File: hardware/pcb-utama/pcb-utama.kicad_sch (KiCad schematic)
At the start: 0 parts

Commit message: Skematik PCB utama lengkap (ERC 0) dari generator
- hardware/tools/gen_sch_utama.py + kisym.py: skematik 5 blok (daya, driver motor, layar/tombol/buzzer, ESP32,
  J5 ke PCB sensor), 21 komponen, footprint terisi; netlist dicek terhadap tabel pin CLAUDE.md (0 salah)
- hardware/pcb-utama/pcb-utama-skematik.pdf
- README PCB utama, CLAUDE.md, handover, log kerja diperbarui

Co-Authored-By: Claude Opus 5.5 <noreply@anthropic.com>
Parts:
- added BZ1: Buzzer aktif 5V, Buzzer_Beeper:Buzzer_12x9.5RM7.6, symbol Device:Buzzer
- added C1: 100uF 16V, Capacitor_THT:CP_Radial_D6.3mm_P2.50mm, symbol Device:C_Polarized
- added D1: 1N5819, Diode_THT:D_DO-41_SOD81_P10.16mm_Horizontal, symbol Device:D_Schottky
- added J1: Baterai (P+/P- BMS), Connector_JST:JST_XH_B2B-XH-A_1x02_P2.50mm_Vertical, symbol Connector_Generic:Conn_01x02
- added J2: Motor kiri + encoder, Connector_JST:JST_PH_B6B-PH-K_1x06_P2.00mm_Vertical, symbol Connector_Generic:Conn_01x06
- added J3: Motor kanan + encoder, Connector_JST:JST_PH_B6B-PH-K_1x06_P2.00mm_Vertical, symbol Connector_Generic:Conn_01x06
- added J4: OLED 0,96 I2C, Connector_PinSocket_2.54mm:PinSocket_1x04_P2.54mm_Vertical, symbol Connector_Generic:Conn_01x04
- added J5: Kabel PCB sensor (= J1 sensor), Connector_JST:JST_XH_B8B-XH-A_1x08_P2.50mm_Vertical, symbol Connector_Generic:Conn_01x08
- added Q1: S8050, Package_TO_SOT_THT:TO-92_Inline, symbol Transistor_BJT:S8050
- added R1: 100k, Resistor_THT:R_Axial_DIN0207_L6.3mm_D2.5mm_P7.62mm_Horizontal, symbol Device:R
- added R2: 33k, Resistor_THT:R_Axial_DIN0207_L6.3mm_D2.5mm_P7.62mm_Horizontal, symbol Device:R
- added R3: 1k, Resistor_THT:R_Axial_DIN0207_L6.3mm_D2.5mm_P7.62mm_Horizontal, symbol Device:R
- added R4, R5, R6: 10k, Resistor_THT:R_Axial_DIN0207_L6.3mm_D2.5mm_P7.62mm_Horizontal, symbol Device:R
- added SW1: Saklar geser, Button_Switch_THT:SW_Slide_SPDT_Angled_CK_OS102011MA1Q, symbol Switch:SW_SPDT
- added SW2: Tombol A, Button_Switch_THT:SW_PUSH_6mm, symbol Switch:SW_Push
- added SW3: Tombol B, Button_Switch_THT:SW_PUSH_6mm, symbol Switch:SW_Push
- added U1: ESP32 DevKit 30 pin, ltm:ESP32_DevKit_30P_W25.4, symbol ltm:ESP32_DevKit_30
- added U2: TB6612 modul, ltm:TB6612_Module_2x8_W15.24, symbol ltm:TB6612_Module
- added U3: MP1584 (set 5,0 V), ltm:MP1584_Module, symbol ltm:MP1584_Module
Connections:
- new net: BZ1.2 (-), Q1.3 (C)
- new net: Q1.2 (B), R3.2, R4.1
- new net +3V3: J2.2 (Pin_2), J3.2 (Pin_2), J4.2 (Pin_2), J5.2 (Pin_2), R5.1, R6.1, U1.30 (3V3), U2.10 (VCC)
- new net +5V: BZ1.1 (+), D1.1 (K), J5.1 (Pin_1), U1.15 (VIN)
- new net +5V_BUCK: D1.2 (A), U3.3 (OUT+)
- new net AIN1: U1.23 (GPIO5), U2.3 (AIN1)
- new net AIN2: U1.24 (GPIO17/TX2), U2.2 (AIN2)
- new net BAT+: J1.1 (Pin_1), SW1.1 (A)
- new net BIN1: U1.26 (GPIO4), U2.5 (BIN1)
- new net BIN2: U1.28 (GPIO15), U2.6 (BIN2)
- new net BTN_A: R5.2, SW2.1, U1.4 (GPIO34)
- new net BTN_B: R6.2, SW3.1, U1.5 (GPIO35)
- new net BUZ: R3.1, U1.12 (GPIO12)
- new net ENC_L_A: J2.3 (Pin_3), U1.13 (GPIO13)
- new net ENC_L_B: J2.4 (Pin_4), U1.11 (GPIO14)
- new net ENC_R_A: J3.3 (Pin_3), U1.16 (GPIO23)
- new net ENC_R_B: J3.4 (Pin_4), U1.21 (GPIO19)
- new net GND: C1.2, J1.2 (Pin_2), J2.5 (Pin_5), J3.5 (Pin_5), J4.1 (Pin_1), J5.3 (Pin_3), Q1.1 (E), R2.2, R4.2, SW2.2, SW3.2, U1.14 (GND), U1.29 (GND), U2.11 (GND), U2.16 (GND), U2.8 (GND), U3.2 (IN-), U3.4 (OUT-)
- new net ML_N: J2.6 (Pin_6), U2.13 (AO2)
- new net ML_P: J2.1 (Pin_1), U2.12 (AO1)
- new net MR_N: J3.6 (Pin_6), U2.14 (BO2)
- new net MR_P: J3.1 (Pin_1), U2.15 (BO1)
- new net MUX_S0: J5.7 (Pin_7), U1.9 (GPIO26)
- new net MUX_S1: J5.6 (Pin_6), U1.8 (GPIO25)
- new net MUX_S2: J5.5 (Pin_5), U1.7 (GPIO33)
- new net MUX_S3: J5.4 (Pin_4), U1.6 (GPIO32)
- new net MUX_SIG: J5.8 (Pin_8), U1.2 (GPIO36/VP)
- new net PWMA: U1.22 (GPIO18), U2.1 (PWMA)
- new net PWMB: U1.25 (GPIO16/RX2), U2.7 (PWMB)
- new net SCL: J4.3 (Pin_3), U1.17 (GPIO22)
- new net SDA: J4.4 (Pin_4), U1.20 (GPIO21)
- new net STBY: U1.27 (GPIO2), U2.4 (STBY)
- new net VBAT: C1.1, R1.1, SW1.2 (B), U2.9 (VM), U3.1 (IN+)
- new net VBAT_SENSE: R1.2, R2.1, U1.3 (GPIO39/VN)
- no-connect marks 0 -> 5
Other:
- note added: "1. DAYA (wiring diagram blok 1)"
- note added: "2. DRIVER MOTOR + MOTOR (wiring diagram blok 2)"
- note added: "3. LAYAR, TOMBOL, BUZZER (wiring diagram blok 3)"
- note added: "4. ESP32 DEVKIT (otak)"
- note added: "5. KABEL KE PCB SENSOR (wiring diagram blok 4)"
- note added: "C1 dekat pin VM TB6612"
- note added: "Cek urutan pin modul OLED (ada yang VCC dulu baru GND)"
- note added: "D1: cegah arus balik saat USB dicolok"
- note added: "Di PCB: J5 sejajar tepi kanan hidung, pin 1 di ujung belakang"
- note added: "EN, GPIO27, TX0, RX0: tidak dipakai (X)"
- note added: "Footprint W25.4: ukur jarak baris pin modul (22,86 mm -> W22.86)"
- note added: "GPIO2 (STBY) dan GPIO12 (BUZ) harus LOW saat boot"
- note added: "GPIO34/35/36/39: hanya input"
- note added: "Ikuti NOMOR pin: pin 4-7 terbalik dari urutan nama (S3 dulu)"
- note added: "J1 = P+/P- BMS (baterai 2S di rangka)"
- note added: "J2/J3 = JST PH 6 pin. Encoder tanpa resistor (firmware INPUT_PULLUP)."
- note added: "J5 = JST XH 8 pin, urutan pin SAMA dengan J1 PCB sensor (kabel lurus, pin n ke pin n)"
- note added: "PWR_FLAG: daya VBAT, +5V, GND datang dari konektor/dioda"
- note added: "Q1 TO-92: cek urutan E-B-C"
- note added: "R4 menjaga GPIO12 LOW saat boot (syarat boot ESP32)"
- note added: "R5/R6 wajib: GPIO34/35 tanpa pull-up internal"
- note added: "SW1: kaki tengah (B) = VBAT"
- note added: "Set MP1584 ke 5,0 V dulu sebelum ESP32 dipasang"
- note added: "Urutan 6 kabel motor N20 beda tiap penjual: cek sebelum crimp."
- note added: "Urutan pin modul TB6612 beda tiap penjual: cocokkan dengan modul yang dibeli."
- note added: "VBAT_SENSE ke GPIO39 (ADC1)"
- note added: "VM = VBAT (7,4 V) langsung, VCC = 3,3 V logika. AO ke motor kiri, BO ke motor kanan."

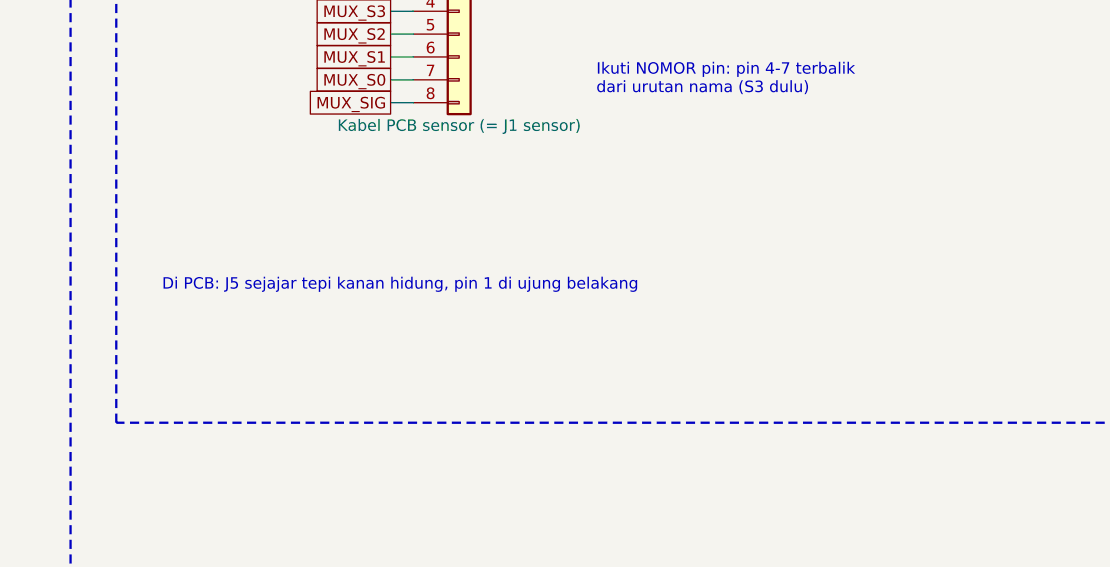
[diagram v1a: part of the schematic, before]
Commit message: Outline PCB utama bentuk mobil F1
Pilihan user dari 3 opsi: sidepod lebar, pinggang lengkung di antara roda,
hidung panjang (100 x 127 mm). J5 pindah ke sidepod kiri (pin 1 dekat
hidung), elko C1 ke sidepod kiri, kabel sensor menyusuri tepi kiri hidung.
Model v16 (0 tabrakan), render, PCB utama (DRC 0), skematik (ERC 0) dan
dokumen diperbarui.

Co-Authored-By: Claude Opus 5.5 <noreply@anthropic.com>
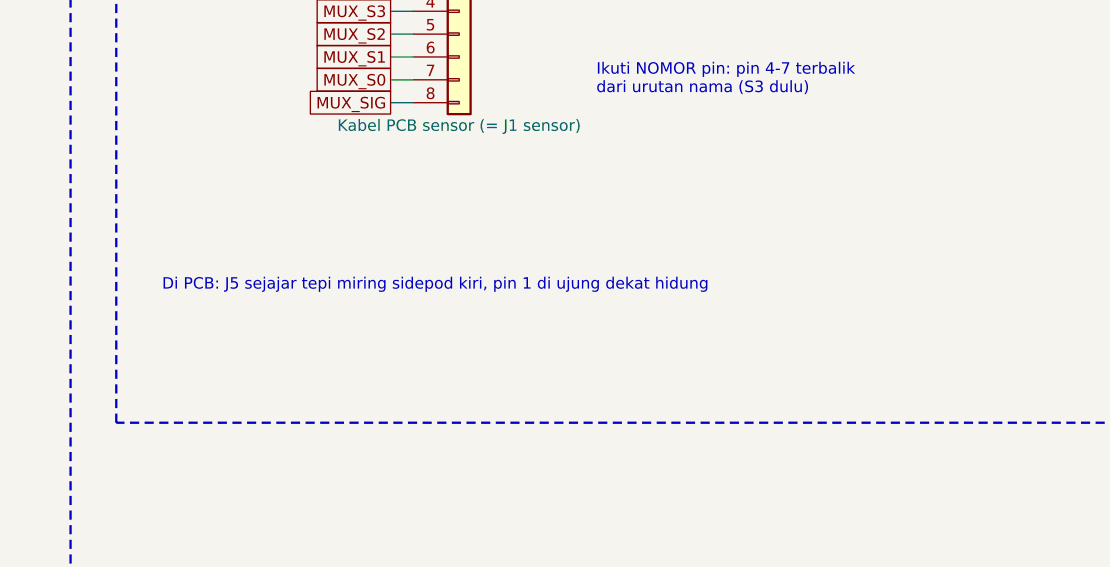
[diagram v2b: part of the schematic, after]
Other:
- note added: "Di PCB: J5 sejajar tepi miring sidepod kiri, pin 1 di ujung dekat hidung"
- note removed: "Di PCB: J5 sejajar tepi kanan hidung, pin 1 di ujung belakang"
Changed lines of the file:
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@@
 	(text "J5 = JST XH 8 pin, urutan pin SAMA\ndengan J1 PCB sensor (kabel lurus,\npin n ke pin n)" (exclude_from_sim no) (at 335.28 147.32 0) (effects (font (size 1.27 1.27)) (justify left)))
 	(text "Ikuti NOMOR pin: pin 4-7 terbalik\ndari urutan nama (S3 dulu)" (exclude_from_sim no) (at 335.28 162.56 0) (effects (font (size 1.27 1.27)) (justify left)))
-	(text "Di PCB: J5 sejajar tepi kanan hidung, pin 1 di ujung belakang" (exclude_from_sim no) (at 287.02 185.42 0) (effects (font (size 1.27 1.27)) (justify left)))
+	(text "Di PCB: J5 sejajar tepi miring sidepod kiri, pin 1 di ujung dekat hidung" (exclude_from_sim no) (at 287.02 185.42 0) (effects (font (size 1.27 1.27)) (justify left)))
 	(symbol (lib_id "Connector_Generic:Conn_01x02") (at 45.72 34.29 0) (unit 1)
 		(exclude_from_sim no) (in_bom yes) (on_board yes) (dnp no)
